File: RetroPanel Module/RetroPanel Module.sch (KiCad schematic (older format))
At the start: 58 parts, among them J1 Front Panel, J10 SW_EXTRA, J16 SPEAKER, J17 LED_HDD, J2 SW_POWER, J3 LED_POWER, J4 SW_RESET, J5 SW_TURBO, J6 LED_TURBO, J7 POWER, J8 IIC, J9 POST_CARD, M1 Mounting_Pin, M10 Mounting_Pad, M11 Mounting_Pad, M12 Mounting_Pad, M13 Mounting_Pad, M14 Mounting_Pad, M15 Mounting_Pad, M16 Mounting_Pin, M2 Mounting_Pin, M3 Mounting_Pin, M4 Mounting_Pad, M5 Mounting_Pad, M6 Mounting_Pad, M7 Mounting_Pad, M8 Mounting_Pad, M9 Mounting_Pad, Q1 2N3904 *, Q2 2N3904 *, Q3 2N3904 *, Q4 2N3904 *

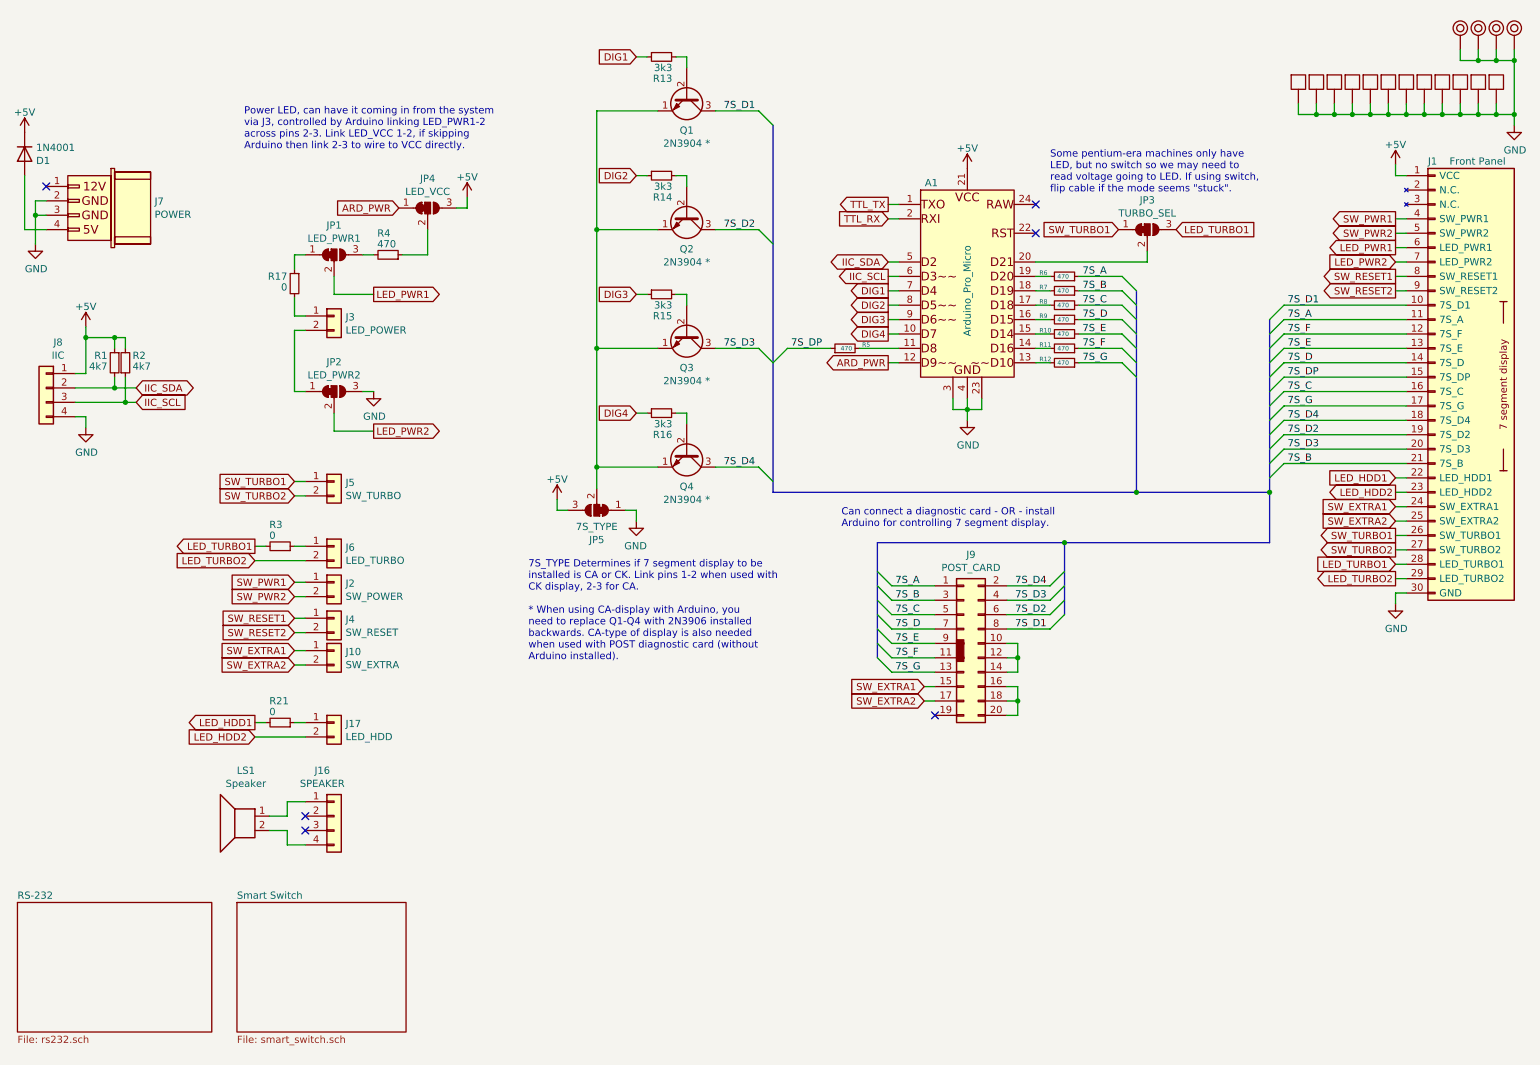
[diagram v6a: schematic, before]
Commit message: Adjustable mounting with huge pads
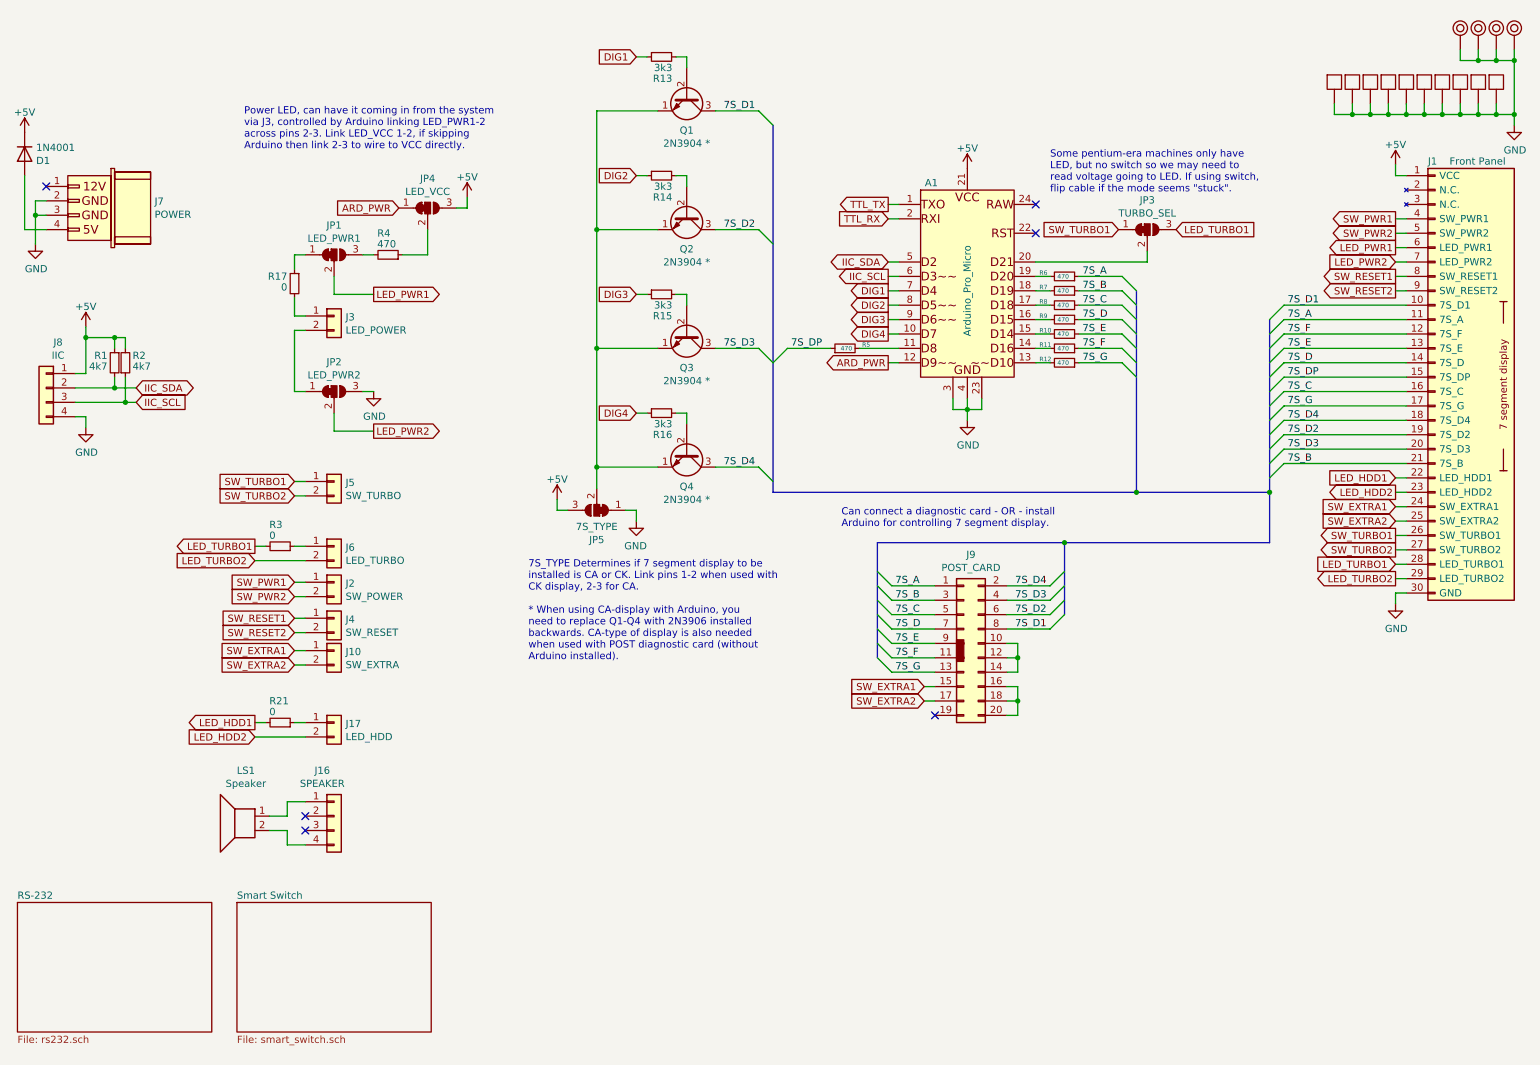
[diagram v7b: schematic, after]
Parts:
- removed M4, M6: Mounting_Pad, RetroPanel:B.Pad_pin, symbol mounting:Mounting_Pad
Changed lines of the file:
@@
 	1    0    0    -1
 $EndComp
-$Comp
-L mounting:Mounting_Pad M6
-U 1 1 637928C6
+Wire Wire Line
+	10950 1150 10950 1225
+Connection ~ 10950 1225
+Wire Wire Line
+	10950 1225 11075 1225
+Wire Wire Line
+	10825 1150 10825 1225
+Connection ~ 10825 1225
+Wire Wire Line
+	10825 1225 10950 1225
+Wire Wire Line
+	10700 1150 10700 1225
+Connection ~ 10700 1225
+Wire Wire Line
+	10700 1225 10825 1225
+$Comp
+L mounting:Mounting_Pad M10
+U 1 1 637AD750
 P 10575 1000
-F 0 "M6" H 10575 1100 50  0001 C CNN
+F 0 "M10" H 10575 1100 50  0001 C CNN
 F 1 "Mounting_Pad" H 10575 925 50  0001 C CNN
-F 2 "RetroPanel:B.Pad_pin" H 10575 1000 50  0001 C CNN
+F 2 "RetroPanel:Pad_pin" H 10575 1000 50  0001 C CNN
 F 3 "~" H 10575 1000 50  0001 C CNN
 	1    10575 1000
 	1    0    0    -1
 $EndComp
-Wire Wire Line
-	10950 1150 10950 1225
-Connection ~ 10950 1225
-Wire Wire Line
-	10950 1225 11075 1225
-Wire Wire Line
-	10825 1150 10825 1225
-Connection ~ 10825 1225
-Wire Wire Line
-	10825 1225 10950 1225
-Wire Wire Line
-	10700 1150 10700 1225
-Connection ~ 10700 1225
-Wire Wire Line
-	10700 1225 10825 1225
-$Comp
-L mounting:Mounting_Pad M10
-U 1 1 637AD750
+$Comp
+L mounting:Mounting_Pad M9
+U 1 1 6359FE8F
 P 10450 1000
-F 0 "M10" H 10450 1100 50  0001 C CNN
+F 0 "M9" H 10450 1100 50  0001 C CNN
 F 1 "Mounting_Pad" H 10450 925 50  0001 C CNN
 F 2 "RetroPanel:Pad_pin" H 10450 1000 50  0001 C CNN
@@
 	1    0    0    -1
 $EndComp
-$Comp
-L mounting:Mounting_Pad M9
-U 1 1 6359FE8F
+Wire Wire Line
+	10450 1150 10450 1225
+Wire Wire Line
+	10575 1150 10575 1225
+Connection ~ 10450 1225
+Connection ~ 11075 850
+Connection ~ 10825 850
+$Comp
+L mounting:Mounting_Pad M11
+U 1 1 635B4DD6
 P 10325 1000
-F 0 "M9" H 10325 1100 50  0001 C CNN
+F 0 "M11" H 10325 1100 50  0001 C CNN
 F 1 "Mounting_Pad" H 10325 925 50  0001 C CNN
 F 2 "RetroPanel:Pad_pin" H 10325 1000 50  0001 C CNN
@@
 Wire Wire Line
 	10325 1150 10325 1225
-Wire Wire Line
-	10325 1225 10450 1225
-Wire Wire Line
-	10450 1150 10450 1225
-Connection ~ 10450 1225
-Wire Wire Line
-	10450 1225 10575 1225
-Wire Wire Line
-	10575 1150 10575 1225
-Connection ~ 10575 1225
-Wire Wire Line
-	10575 1225 10700 1225
-Connection ~ 11075 850
-Connection ~ 10825 850
-$Comp
-L mounting:Mounting_Pad M4
-U 1 1 635B1EEE
+$Comp
+L mounting:Mounting_Pad M12
+U 1 1 635B6874
 P 10200 1000
-F 0 "M4" H 10200 1100 50  0001 C CNN
+F 0 "M12" H 10200 1100 50  0001 C CNN
 F 1 "Mounting_Pad" H 10200 925 50  0001 C CNN
-F 2 "RetroPanel:B.Pad_pin" H 10200 1000 50  0001 C CNN
+F 2 "RetroPanel:Pad_pin" H 10200 1000 50  0001 C CNN
 F 3 "~" H 10200 1000 50  0001 C CNN
 	1    10200 1000
@@
 	10200 1150 10200 1225
 Wire Wire Line
-	10325 1225 10200 1225
-Connection ~ 10325 1225
-$Comp
-L mounting:Mounting_Pad M11
-U 1 1 635B4DD6
+	9950 1225 10075 1225
+Connection ~ 10075 1225
+$Comp
+L mounting:Mounting_Pad M13
+U 1 1 635B7F85
 P 10075 1000
-F 0 "M11" H 10075 1100 50  0001 C CNN
+F 0 "M13" H 10075 1100 50  0001 C CNN
 F 1 "Mounting_Pad" H 10075 925 50  0001 C CNN
 F 2 "RetroPanel:Pad_pin" H 10075 1000 50  0001 C CNN
@@
 Wire Wire Line
 	10075 1150 10075 1225
-Wire Wire Line
-	10075 1225 10200 1225
-Connection ~ 10200 1225
-$Comp
-L mounting:Mounting_Pad M12
-U 1 1 635B6874
-P 9950 1000
-F 0 "M12" H 9950 1100 50  0001 C CNN
-F 1 "Mounting_Pad" H 9950 925 50  0001 C CNN
-F 2 "RetroPanel:Pad_pin" H 9950 1000 50  0001 C CNN
-F 3 "~" H 9950 1000 50  0001 C CNN
-	1    9950 1000
-	1    0    0    -1
-$EndComp
-Wire Wire Line
-	9950 1150 9950 1225
-Wire Wire Line
-	9950 1225 10075 1225
-Connection ~ 10075 1225
-$Comp
-L mounting:Mounting_Pad M13
-U 1 1 635B7F85
-P 9825 1000
-F 0 "M13" H 9825 1100 50  0001 C CNN
-F 1 "Mounting_Pad" H 9825 925 50  0001 C CNN
-F 2 "RetroPanel:Pad_pin" H 9825 1000 50  0001 C CNN
-F 3 "~" H 9825 1000 50  0001 C CNN
-	1    9825 1000
-	1    0    0    -1
-$EndComp
-Wire Wire Line
-	9825 1150 9825 1225
 Wire Wire Line
 	9825 1225 9950 1225
@@
 L mounting:Mounting_Pad M14
 U 1 1 635E064A
-P 9700 1000
-F 0 "M14" H 9700 1100 50  0001 C CNN
-F 1 "Mounting_Pad" H 9700 925 50  0001 C CNN
-F 2 "RetroPanel:B.Pad_pin" H 9700 1000 50  0001 C CNN
-F 3 "~" H 9700 1000 50  0001 C CNN
-	1    9700 1000
-	1    0    0    -1
-$EndComp
-Wire Wire Line
-	9700 1150 9700 1225
-Wire Wire Line
-	9700 1225 9825 1225
-Connection ~ 9825 1225
+P 9950 1000
+F 0 "M14" H 9950 1100 50  0001 C CNN
+F 1 "Mounting_Pad" H 9950 925 50  0001 C CNN
+F 2 "RetroPanel:B.Pad_pin" H 9950 1000 50  0001 C CNN
+F 3 "~" H 9950 1000 50  0001 C CNN
+	1    9950 1000
+	1    0    0    -1
+$EndComp
+Wire Wire Line
+	9950 1150 9950 1225
 $Comp
 L mounting:Mounting_Pad M15
 U 1 1 635E5F23
-P 9575 1000
-F 0 "M15" H 9575 1100 50  0001 C CNN
-F 1 "Mounting_Pad" H 9575 925 50  0001 C CNN
-F 2 "RetroPanel:Pad_pin" H 9575 1000 50  0001 C CNN
-F 3 "~" H 9575 1000 50  0001 C CNN
-	1    9575 1000
-	1    0    0    -1
-$EndComp
-Wire Wire Line
-	9575 1150 9575 1225
-Wire Wire Line
-	9575 1225 9700 1225
-Connection ~ 9700 1225
+P 9825 1000
+F 0 "M15" H 9825 1100 50  0001 C CNN
+F 1 "Mounting_Pad" H 9825 925 50  0001 C CNN
+F 2 "RetroPanel:Pad_pin" H 9825 1000 50  0001 C CNN
+F 3 "~" H 9825 1000 50  0001 C CNN
+	1    9825 1000
+	1    0    0    -1
+$EndComp
+Wire Wire Line
+	9825 1150 9825 1225
 $Comp
 L mounting:Mounting_Pin M16
@@
 $EndSheet
 $Sheet
-S 2200 6700 1175 900
+S 2200 6700 1350 900
 U 63655027
 F0 "Smart Switch" 50
@@
 	0    -1   1    0
 $EndComp
+$Comp
+L Transistor_BJT:2N3904 Q2
+U 1 1 6409DF7D
+P 5325 1925
+F 0 "Q2" V 5560 1925 50  0000 C CNN
+F 1 "2N3904 *" V 5651 1925 50  0000 C CNN
+F 2 "Package_TO_SOT_THT:TO-92_Inline_Wide" H 5525 1850 50  0001 L CIN
+F 3 "https://www.onsemi.com/pub/Collateral/2N3903-D.PDF" H 5325 1925 50  0001 L CNN
+	1    5325 1925
+	0    1    1    0
+$EndComp
+Wire Wire Line
+	10075 1225 10200 1225
+Wire Wire Line
+	10450 1225 10575 1225
+Connection ~ 10200 1225
+Connection ~ 10575 1225
+Wire Wire Line
+	10575 1225 10700 1225
+Wire Wire Line
+	10200 1225 10325 1225
+Connection ~ 10325 1225
+Wire Wire Line
+	10325 1225 10450 1225
 Wire Bus Line
 	7950 4200 7950 4700
@@
 Wire Bus Line
 	9375 2650 9375 3850
-$Comp
-L Transistor_BJT:2N3904 Q2
-U 1 1 6409DF7D
-P 5325 1925
-F 0 "Q2" V 5560 1925 50  0000 C CNN
-F 1 "2N3904 *" V 5651 1925 50  0000 C CNN
-F 2 "Package_TO_SOT_THT:TO-92_Inline_Wide" H 5525 1850 50  0001 L CIN
-F 3 "https://www.onsemi.com/pub/Collateral/2N3903-D.PDF" H 5325 1925 50  0001 L CNN
-	1    5325 1925
-	0    1    1    0
-$EndComp
 $EndSCHEMATC

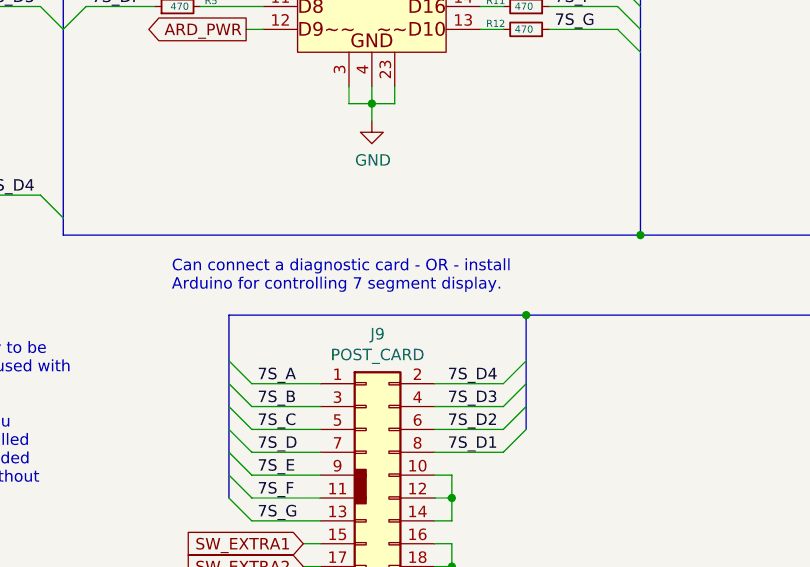
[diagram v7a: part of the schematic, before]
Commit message: Fixed RS-232 connector and export files for second prototype
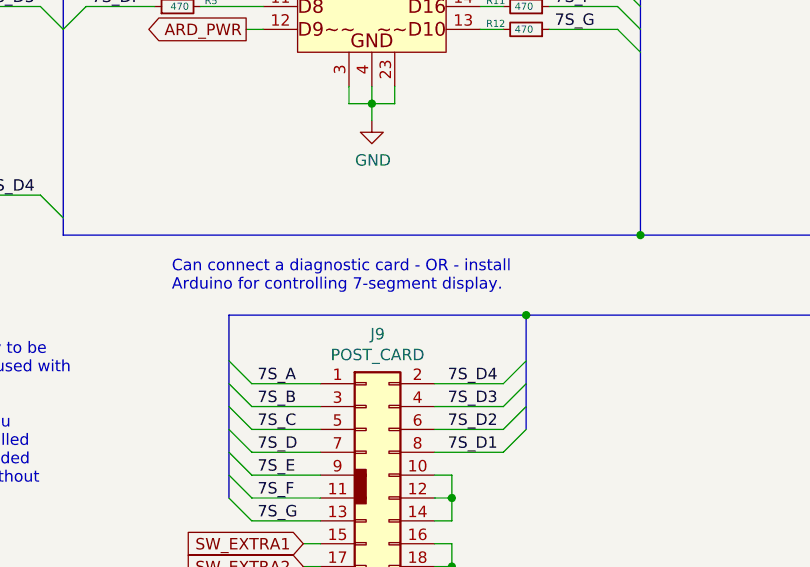
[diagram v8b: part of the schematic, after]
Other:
- note added: "Can connect a diagnostic card - OR - install\nArduino for controlling 7-segment display."
- note removed: "Can connect a diagnostic card - OR - install\nArduino for controlling 7 segment display."
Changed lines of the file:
@@
 Some pentium-era machines only have\nLED, but no switch so we may need to\nread voltage going to LED. If using switch,\nflip cable if the mode seems "stuck".
 Text Notes 6400 4100 0    50   ~ 0
-Can connect a diagnostic card - OR - install\nArduino for controlling 7 segment display.
+Can connect a diagnostic card - OR - install\nArduino for controlling 7-segment display.
 $Comp
 L solder_select:SolderJumper_3_Bridged12 JP4
